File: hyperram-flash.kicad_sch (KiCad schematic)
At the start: 17 parts, among them U1 IS66WVH16M8DALL-166B1LI, U27 W25Q128JWEIQ

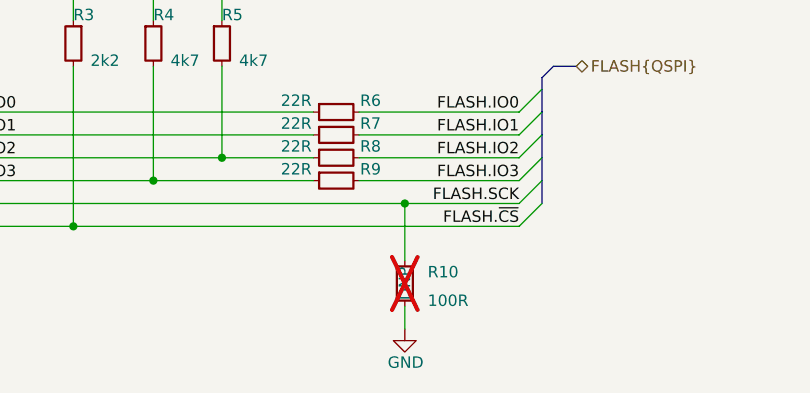
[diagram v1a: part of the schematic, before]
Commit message: [#69629] Fix DNP attributes
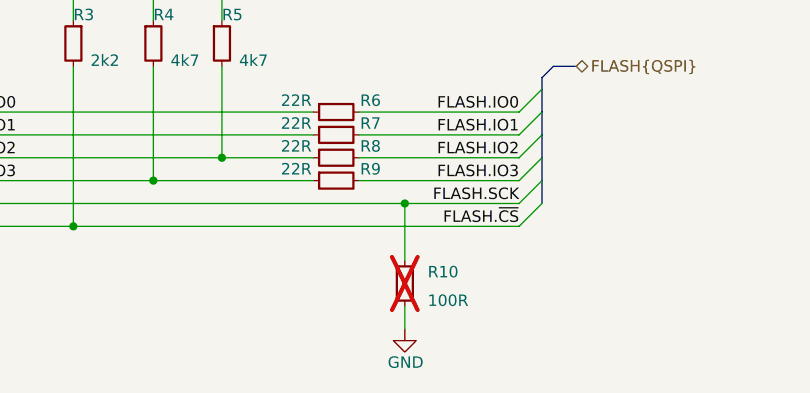
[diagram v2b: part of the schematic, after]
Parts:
- R10: DNP DNP -> (none)
